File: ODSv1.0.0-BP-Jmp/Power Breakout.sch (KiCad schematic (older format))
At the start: 3 parts, among them J4 Conn_02x10_Odd_Even, J5 Conn_02x10_Odd_Even, J6 Conn_02x10_Odd_Even

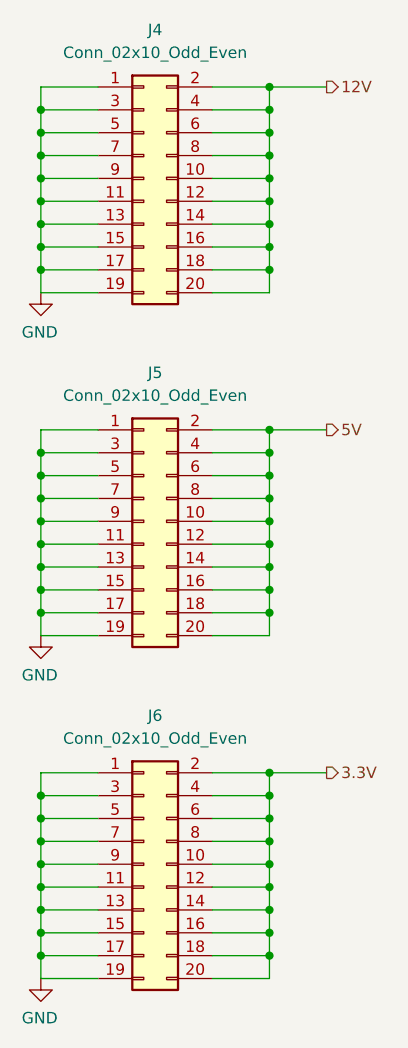
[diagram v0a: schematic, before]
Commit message: Fix hierarchical pin label directions, finish front right corner
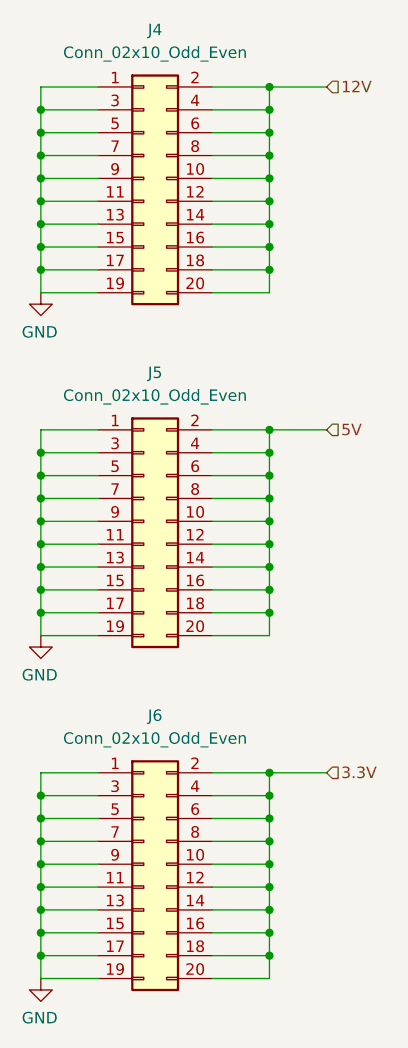
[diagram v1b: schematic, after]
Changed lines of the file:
@@
 Comment4 "Octopi Driver Stack v1.0.0: Plane"
 $EndDescr
-Text HLabel 3000 2500 2    50   Output ~ 0
+Text HLabel 3000 2500 2    50   Input ~ 0
 5V
-Text HLabel 3000 4000 2    50   Output ~ 0
+Text HLabel 3000 4000 2    50   Input ~ 0
 3.3V
-Text HLabel 3000 1000 2    50   Output ~ 0
+Text HLabel 3000 1000 2    50   Input ~ 0
 12V
 Wire Wire Line
